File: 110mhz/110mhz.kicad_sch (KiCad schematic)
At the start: 13 parts, among them J1 In, J2 Out

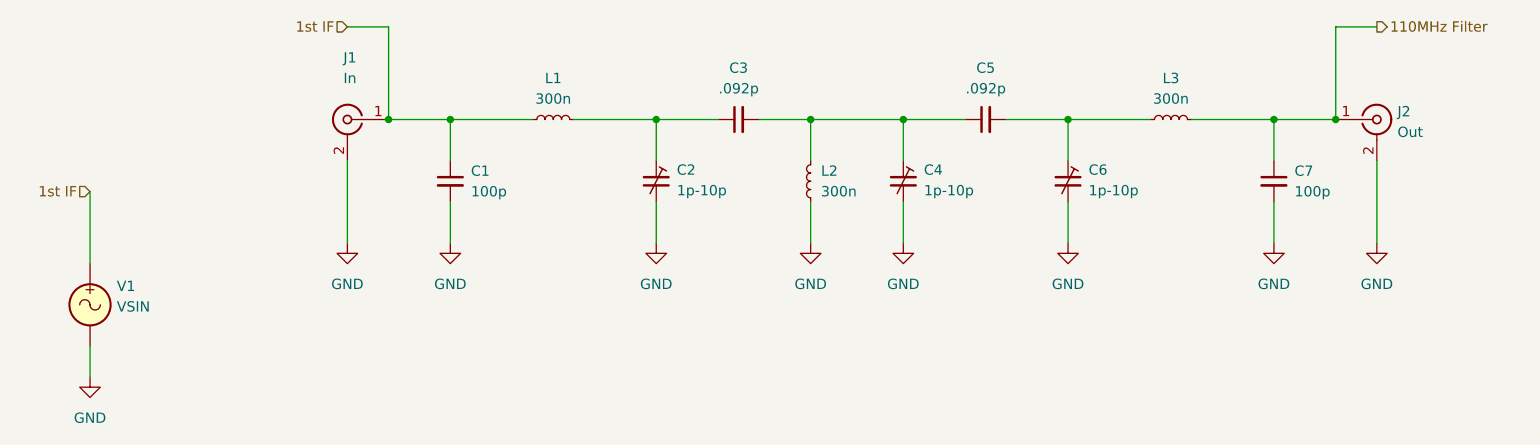
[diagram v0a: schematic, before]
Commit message: updates to hierarchical schematic
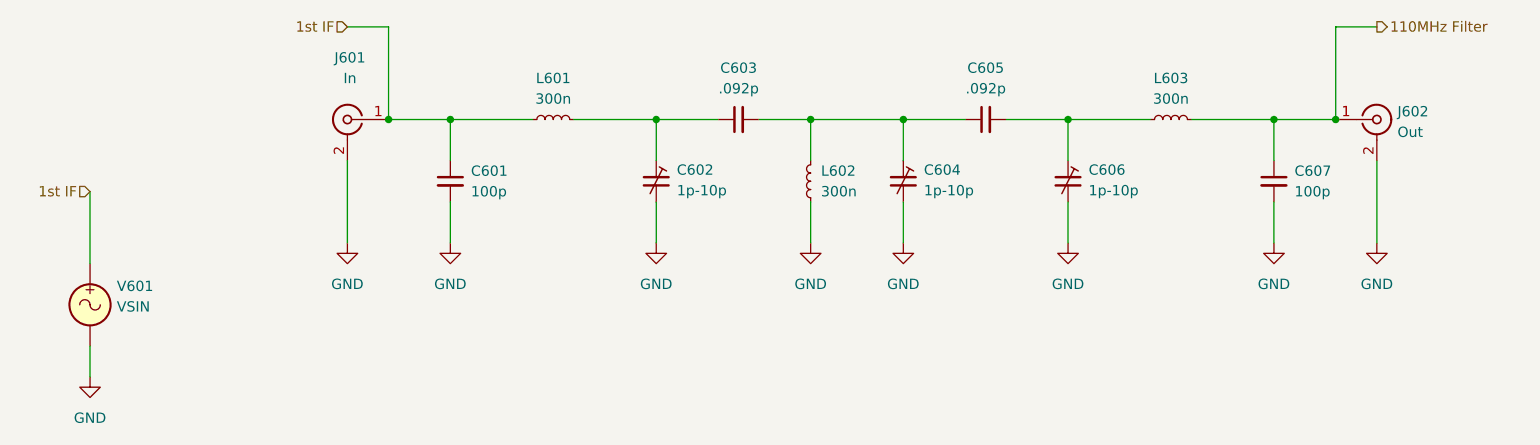
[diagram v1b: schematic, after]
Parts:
- renumbered C1 to C601, C2 to C602, C3 to C603, C4 to C604, C5 to C605, C6 to C606, C7 to C607, J1 to J601, J2 to J602, L1 to L601, L2 to L602, L3 to L603, V1 to V601
